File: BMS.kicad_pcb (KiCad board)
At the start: 2 copper layers, 93 x 75 mm, 17 parts, among them CN001 CN001, CN003 S04B-ZESK-2D_T__LF__SN_, CN004 S04B-ZESK-2D_T__LF__SN_, CN2 CN002, IC1 TPS7A1633DGNT, J1 -, J2 Rx, J3 Tx, J4 +, Q006 ATP304-TL-H, Q007 ATP304-TL-H, Q008 ATP304-TL-H, Q009 ATP304-TL-H, Q010 ATP304-TL-H, Q011 ATP304-TL-H, U1 BQ77PL900DL

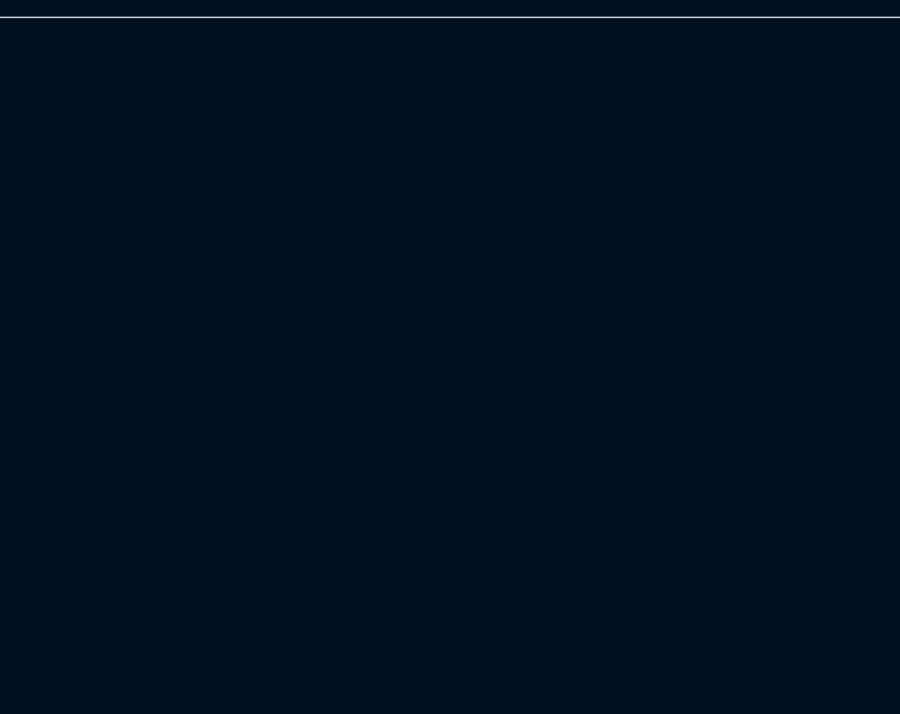
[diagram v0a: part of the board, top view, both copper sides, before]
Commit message: Added possible IC003 pinout to README.
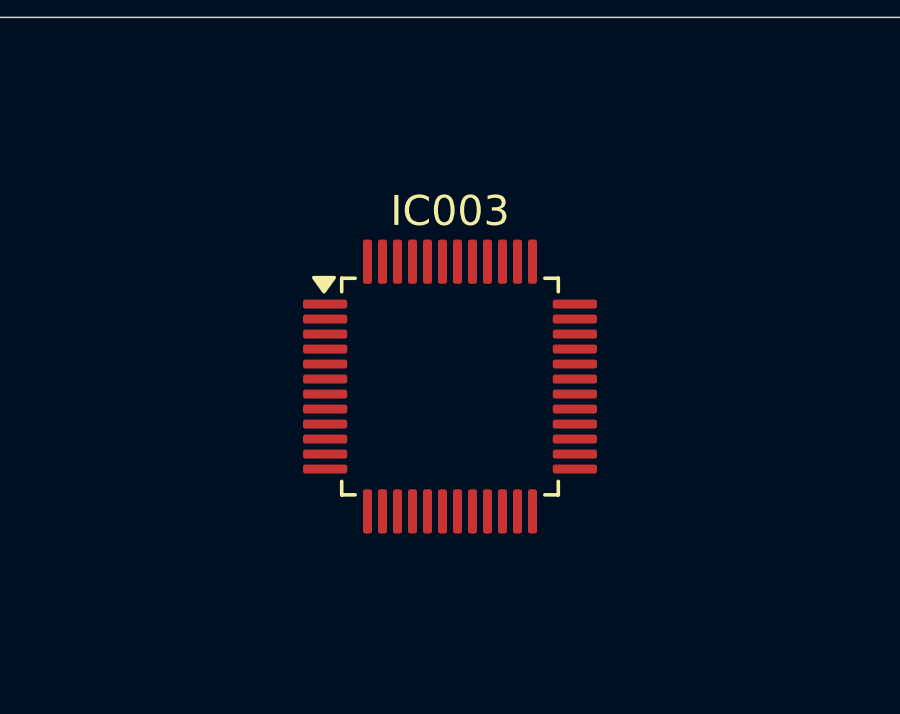
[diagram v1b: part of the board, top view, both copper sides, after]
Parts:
- added IC003: R7FS12878xA01CFL, Package_QFP:LQFP-48_7x7mm_P0.5mm, F.Cu at (171.4, 53.5)
- renumbered IC1 to IC002
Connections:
- net /CHARGER_P renamed /PACK_P
- net Net-(D006-A) renamed /CHG_GATES
- IC002 pad 1: unconnected-(IC1-OUT-Pad1) -> /LDO_OUT
- IC002 pad 2: unconnected-(IC1-FB/DNC-Pad2) -> /LDO_FB
- IC002 pad 3: unconnected-(IC1-PG-Pad3) -> /LDO_PG
- IC002 pad 4: unconnected-(IC1-GND-Pad4) -> GND
- IC002 pad 5: unconnected-(IC1-EN-Pad5) -> /LDO_EN
- IC002 pad 7: unconnected-(IC1-DELAY-Pad7) -> /LDO_DELAY
- IC002 pad 8: unconnected-(IC1-IN-Pad8) -> /LDO_IN
- J2 pad 1: unconnected-(J2-Pin_1-Pad1) -> Net-(J2-Pin_1)
- J3 pad 1: unconnected-(J3-Pin_1-Pad1) -> Net-(J3-Pin_1)
- U1 pad 1: unconnected-(U1-CPOUT-Pad1) -> /CPOUT
- U1 pad 21: unconnected-(U1-GND-Pad21) -> GND
- U1 pad 22: unconnected-(U1-SRBGND-Pad22) -> /SRBGND
- U1 pad 23: unconnected-(U1-SRPGND-Pad23) -> /SRPGND
- U1 pad 24: unconnected-(U1-EEPROM-Pad24) -> /EEPROM
- U1 pad 25: unconnected-(U1-XALERT-Pad25) -> /IC003_PIN14
- U1 pad 26: unconnected-(U1-SDATA-Pad26) -> /SDATA
- U1 pad 27: unconnected-(U1-SCLK-Pad27) -> /SCLK
- U1 pad 28: unconnected-(U1-XRST-Pad28) -> /XRST
- U1 pad 29: unconnected-(U1-IOUT-Pad29) -> GND
- U1 pad 3: unconnected-(U1-CP4-Pad3) -> GND
- U1 pad 30: unconnected-(U1-GND-Pad30) -> GND
- U1 pad 31: unconnected-(U1-VOUT-Pad31) -> /VOUT
- U1 pad 32: unconnected-(U1-VLOG-Pad32) -> /VLOG
- U1 pad 33: unconnected-(U1-CNF0-Pad33) -> GND
- U1 pad 34: unconnected-(U1-CNF1-Pad34) -> GND
- U1 pad 35: unconnected-(U1-CNF2-Pad35) -> GND
- U1 pad 36: unconnected-(U1-ZEDE-Pad36) -> GND
- U1 pad 37: unconnected-(U1-GND-Pad37) -> GND
- U1 pad 38: unconnected-(U1-TIN-Pad38) -> /TIN
- U1 pad 39: unconnected-(U1-TOUT-Pad39) -> /TIN
- U1 pad 4: unconnected-(U1-CP3-Pad4) -> /CP3
- U1 pad 40: unconnected-(U1-VREG2-Pad40) -> /VLOG
- U1 pad 41: unconnected-(U1-GND-Pad41) -> GND
- U1 pad 42: unconnected-(U1-VREG1-Pad42) -> /VREG1
- U1 pad 46: unconnected-(U1-PMS-Pad46) -> /PMS
- U1 pad 47: unconnected-(U1-PACK-Pad47) -> /PACK
- U1 pad 5: unconnected-(U1-CP2-Pad5) -> /CP2
- U1 pad 6: unconnected-(U1-CP1-Pad6) -> /CP1
